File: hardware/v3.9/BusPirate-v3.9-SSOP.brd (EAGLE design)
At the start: 50 x 50 mm, 43 parts, among them CON1 CON_JST_PH_10, CON2 CON_JST_PH_6, CON3 CON-USB-F-MICRO-B, IC1 PIC24FJ64GA002, IC3 4066, IC4 IC_FT230X-SSOP-16

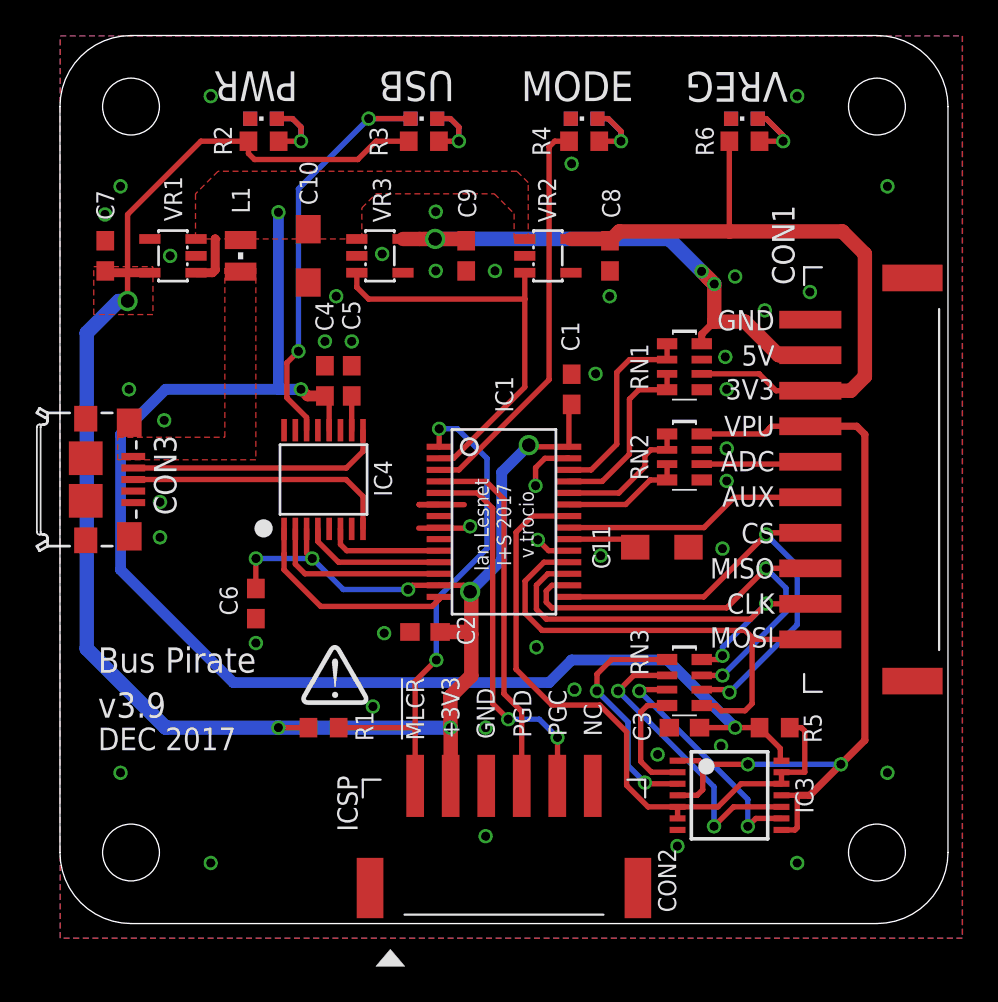
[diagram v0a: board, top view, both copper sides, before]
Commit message: - Change IO connector to 0.1 PTH right angled shrouded - Change USB connector - Change LEDs from 0603 to 0804 - Fix texts orientation
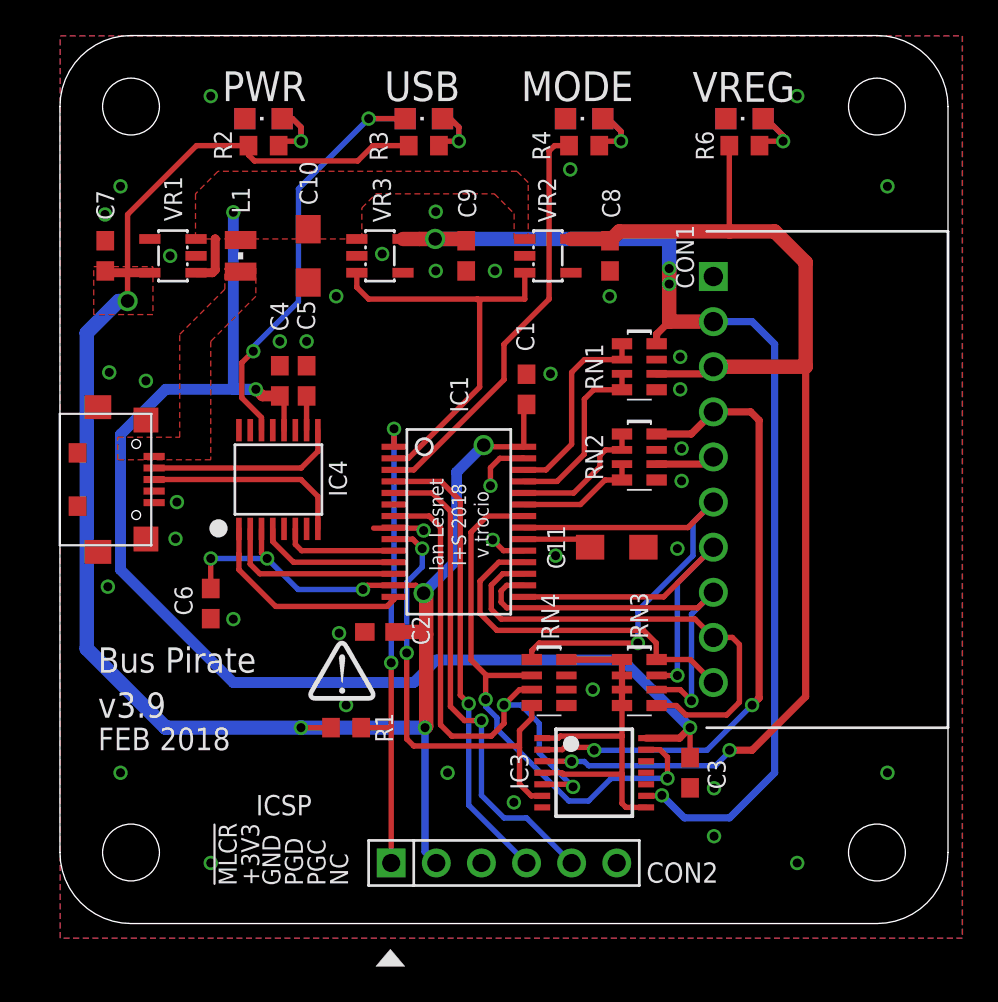
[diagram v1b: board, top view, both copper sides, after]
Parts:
- removed R5: 10K, dp_devices:R603
- added RN4: 10k, dp_devices:RN8P-4R-CRA06S
- CON1: value CON_JST_PH_10 -> CON_HEADER_1X10-RIGHT_ANGLED_PTH_SHROUDED; device dp_devices.v6:CON_JST_PH_SMD_10 -> dp_devices.v6:M1X10_MALE_RIGHT_ANGLES_PTH_SHROUDED
- CON2: value CON_JST_PH_6 -> CON_HEADER_1X06-PTH; device dp_devices.v6:CON_JST_PH_SMD_6 -> dp_devices.v6:M1X6
- CON3: device dp_devices.v6:CONN_USB_MICRO-B -> dp_devices.v6:CON_USB_MICRO-B-1-MD05SMXXX-01
- LED1, LED1A, LED2, LED2A, LED3, LED3A, LED4, LED4A: device dp_devices:LED-603 -> dp_devices.v6:LED-805
- moved IC3 7.73 mm to (30.5, 8.89)
- moved CON2 6.35 mm to (19.1, 3.81), turned to 0 degrees
- moved CON1 3.30 mm to (43.6, 25.4)
- moved C3 2.56 mm to (35.9, 8.89), turned to 270 degrees
- moved C4 2.54 mm to (12.8, 31.0)
- moved C5 2.54 mm to (14.3, 31.0)
- moved IC4 2.54 mm to (12.7, 25.4)
- moved C1 2.54 mm to (26.7, 30.5)
- moved C11 2.54 mm to (31.8, 21.6)
- moved C2 2.54 mm to (18.4, 16.8)
- moved C6 2.54 mm to (8.89, 18.4)
- moved IC1 2.54 mm to (22.9, 23.0)
- moved RN1 2.54 mm to (33.0, 31.8)
- moved RN2 2.54 mm to (33.0, 26.7)
- moved RN3 2.54 mm to (33.0, 14.0)
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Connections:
- removed net N$1: IC3.2, RN3.4
- removed net N$2: IC3.9, RN3.3
- removed net N$4: IC3.10, RN3.2
- removed net N$5: IC3.3, RN3.1
- removed net TP0: IC1.9
- new net N$10: IC3.1, IC3.4, IC3.8, RN3.1, RN3.2, RN3.3, RN3.4, RN4.8
- new net TP1: IC1.6
- new net V33PU: IC1.7, IC3.5, RN4.3
- new net V50PU: IC1.9, IC3.6, RN4.4
- net +3V3: now also CON2.2; no longer CON2.P2
- net ADC: now also CON1.5; no longer CON1.P6
- net AUX1: now also CON1.6, RN4.1; no longer CON1.P5
- net CLK: now also CON1.9, RN3.5; no longer CON1.P2, RN3.8
- net CS: now also CON1.7, RN3.7; no longer CON1.P4, RN3.6
- net GND: now also CON1.1, CON2.3, CON3.GND1, CON3.GND2, CON3.GND3, CON3.GND4, CON3.GND5, CON3.GND6, RN4.5, RN4.6, RN4.7; no longer CON1.G1, CON1.G2, CON1.P10, CON2.G1, CON2.G2, CON2.P3, CON3.BODY@1, CON3.BODY@2, CON3.BODY@3, CON3.BODY@6, IC1.6, IC1.7
- net MCLR: now also CON2.1; no longer CON2.P1
- net MISO: now also CON1.8, RN3.6; no longer CON1.P3, RN3.7
- net MOSI: now also CON1.10, RN3.8; no longer CON1.P1, RN3.5
- net PGC: now also CON2.5; no longer CON2.P5
- net PGD: now also CON2.4; no longer CON2.P4
- net PULLUPEN: now also RN4.2; no longer IC3.12, IC3.5, IC3.6, R5.2
- net SWV33: now also CON1.3, IC3.3; no longer CON1.P8
- net SWV50: now also CON1.2, IC3.9; no longer CON1.P9
- net VEXTERN: now also CON1.4, IC3.2; no longer CON1.P7, IC3.1, IC3.11, IC3.4, IC3.8
- net VUSB: no longer R5.1
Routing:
- net SWV50: track 32.0 -> 63.5 mm, vias 3 -> 4
- net V33PU: track 0.00 -> 29.7 mm, vias 0 -> 2
- net SWV33: track 39.2 -> 68.6 mm, vias 0 -> 2
- net V50PU: track 0.00 -> 25.7 mm, vias 0 -> 2
- net N$10: track 0.00 -> 21.7 mm
- net N$4: track 17.2 -> 0.00 mm, vias 2 -> 0
- net N$2: track 13.8 -> 0.00 mm, vias 2 -> 0
- net N$5: track 13.4 -> 0.00 mm, vias 2 -> 0
- net AUX1: track 14.3 -> 27.6 mm, vias 0 -> 1
- net VEXTERN: track 47.8 -> 35.7 mm
- net MOSI: track 28.2 -> 20.0 mm
- net CS: track 27.9 -> 21.1 mm, vias 2 -> 1
- net N$1: track 6.74 -> 0.00 mm
- net VUSB: track 81.7 -> 75.2 mm
- net PGC: track 21.6 -> 27.5 mm, vias 2 -> 1
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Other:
- board text added: "FEB 2018"
- board text added: "I+S 2018"
- board text removed: "DEC 2017"
- board text removed: "I+S 2017"
